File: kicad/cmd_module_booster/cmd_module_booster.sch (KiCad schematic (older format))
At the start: 15 parts, among them J1 Rails, J2 Power, J3 RPi Connect, U1 LMD18200

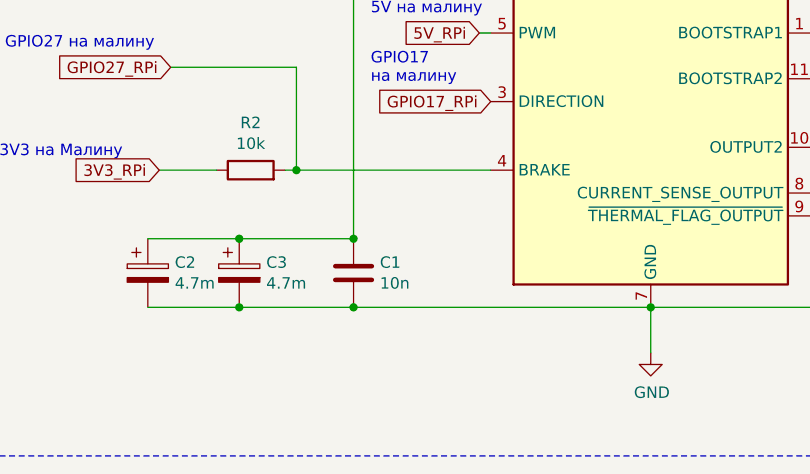
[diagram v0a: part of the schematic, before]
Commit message: Change power supply capacitor
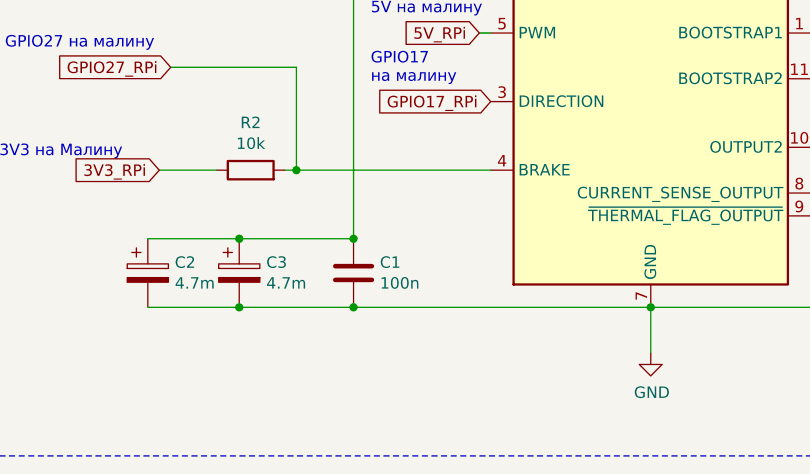
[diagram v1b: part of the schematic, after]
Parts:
- C1: value 10n -> 100n
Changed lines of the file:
@@
 P 2575 3075
 F 0 "C1" H 2690 3121 50  0000 L CNN
-F 1 "10n" H 2690 3030 50  0000 L CNN
+F 1 "100n" H 2690 3030 50  0000 L CNN
 F 2 "Capacitor_THT:C_Disc_D3.0mm_W1.6mm_P2.50mm" H 2613 2925 50  0001 C CNN
 F 3 "~" H 2575 3075 50  0001 C CNN
